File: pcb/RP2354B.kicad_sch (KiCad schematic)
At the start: 29 parts, among them J1 Conn_01x03_MountingPin, SW1 SW_Push, SW2 SW_Push, U2 RP2354B, Y1 ABM8-272-T3

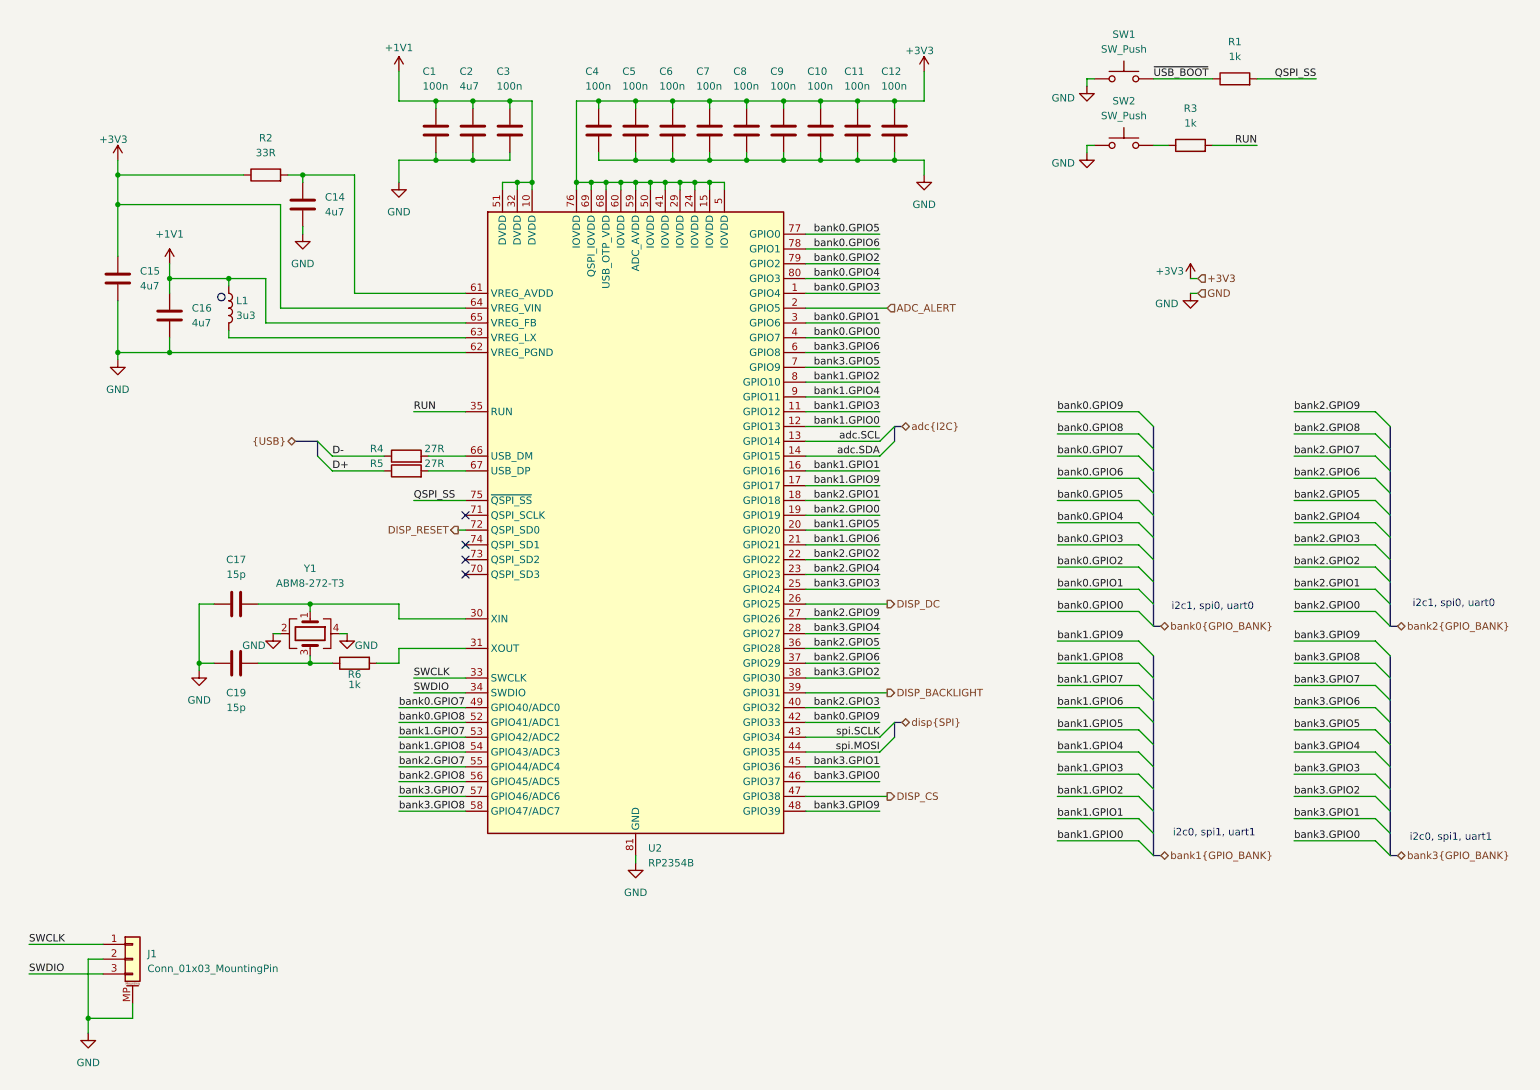
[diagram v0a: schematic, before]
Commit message: finished rough schematic
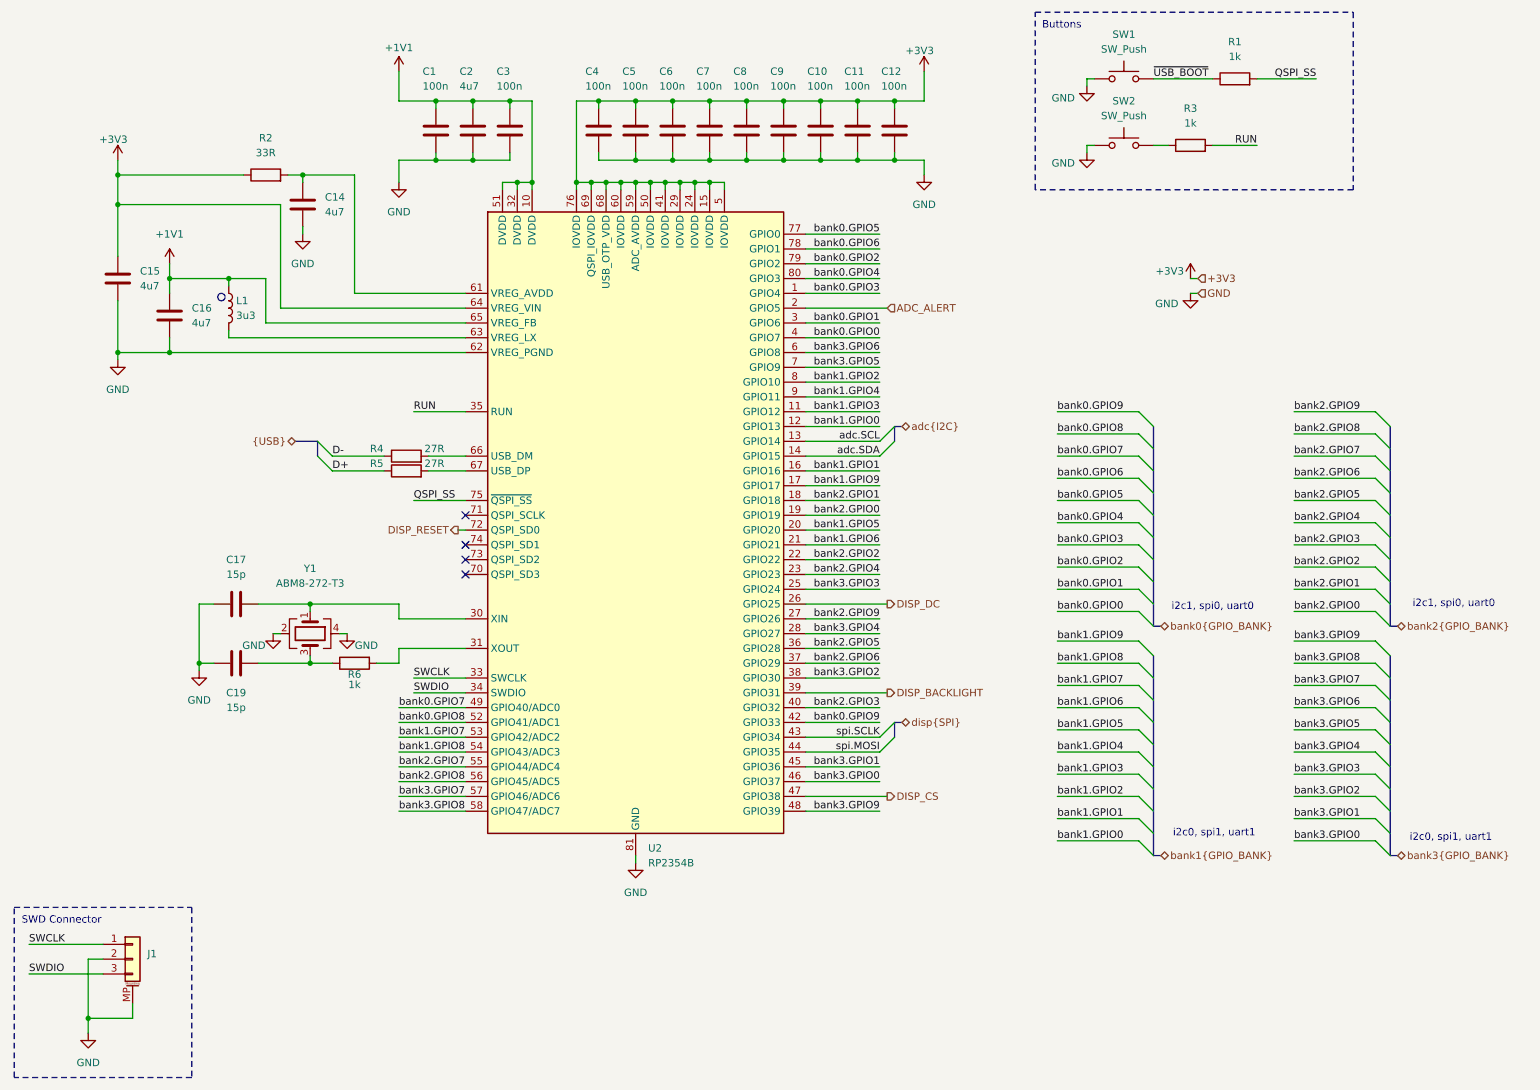
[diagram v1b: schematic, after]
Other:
- note added: "Buttons"
- note added: "SWD Connector"
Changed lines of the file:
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@@
 	(generator_version "10.0")
 	(paper "A4")
+	(rectangle
+		(start 189.23 13.97)
+		(end 243.84 44.45)
+		(stroke
+			(width 0.2032)
+			(type dash)
+		)
+		(fill
+			(type none)
+		)
+	)
+	(rectangle
+		(start 13.97 167.64)
+		(end 44.45 196.85)
+		(stroke
+			(width 0.2032)
+			(type dash)
+		)
+		(fill
+			(type none)
+		)
+	)
 	(circle
 		(center 49.53 62.865)
@@
 		)
 	)
+	(text "Buttons"
+		(exclude_from_sim no)
+		(at 193.802 16.256 0)
+		(effects
+			(font
+				(size 1.27 1.27)
+			)
+		)
+	)
 	(text "i2c1, spi0, uart0"
 		(exclude_from_sim no)
@@
 		)
 	)
+	(text "SWD Connector"
+		(exclude_from_sim no)
+		(at 22.098 169.926 0)
+		(effects
+			(font
+				(size 1.27 1.27)
+			)
+		)
+	)
 	(junction
 		(at 99.06 29.21)
@@
 		(property "Value" "Conn_01x03_MountingPin"
 			(at 36.83 178.1555 0)
+			(hide yes)
 			(show_name no)
 			(do_not_autoplace no)

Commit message: did more layout, added 3d models
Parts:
- R1, R3: footprint Resistor_SMD:R_0603_1608Metric -> Resistor_SMD:R_0402_1005Metric
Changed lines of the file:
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@@
 			)
 		)
-		(property "Footprint" "Resistor_SMD:R_0603_1608Metric"
+		(property "Footprint" "Resistor_SMD:R_0402_1005Metric"
 			(at 223.52 27.178 90)
 			(hide yes)
@@
 			)
 		)
-		(property "Footprint" "Resistor_SMD:R_0603_1608Metric"
+		(property "Footprint" "Resistor_SMD:R_0402_1005Metric"
 			(at 215.9 38.608 90)
 			(hide yes)

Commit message: changed out footprints
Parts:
- C15, C16: footprint Capacitor_SMD:C_0402_1005Metric -> RP2354B_MINIMAL:C_0402_1005Metric_small_pads
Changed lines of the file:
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@@
 			)
 		)
-		(property "Footprint" "Capacitor_SMD:C_0402_1005Metric"
+		(property "Footprint" "RP2354B_MINIMAL:C_0402_1005Metric_small_pads"
 			(at 32.7152 63.5 0)
 			(hide yes)
@@
 			)
 		)
-		(property "Footprint" "Capacitor_SMD:C_0402_1005Metric"
+		(property "Footprint" "RP2354B_MINIMAL:C_0402_1005Metric_small_pads"
 			(at 41.6052 69.85 0)
 			(hide yes)

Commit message: worked on the pcb
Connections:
- net spi.MOSI renamed disp.MOSI
- net spi.SCLK renamed disp.SCLK
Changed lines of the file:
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@@
 		)
 	)
-	(label "spi.SCLK"
+	(label "disp.SCLK"
 		(at 162.56 138.43 180)
 		(effects
@@
 		)
 	)
-	(label "spi.MOSI"
+	(label "disp.MOSI"
 		(at 162.56 140.97 180)
 		(effects

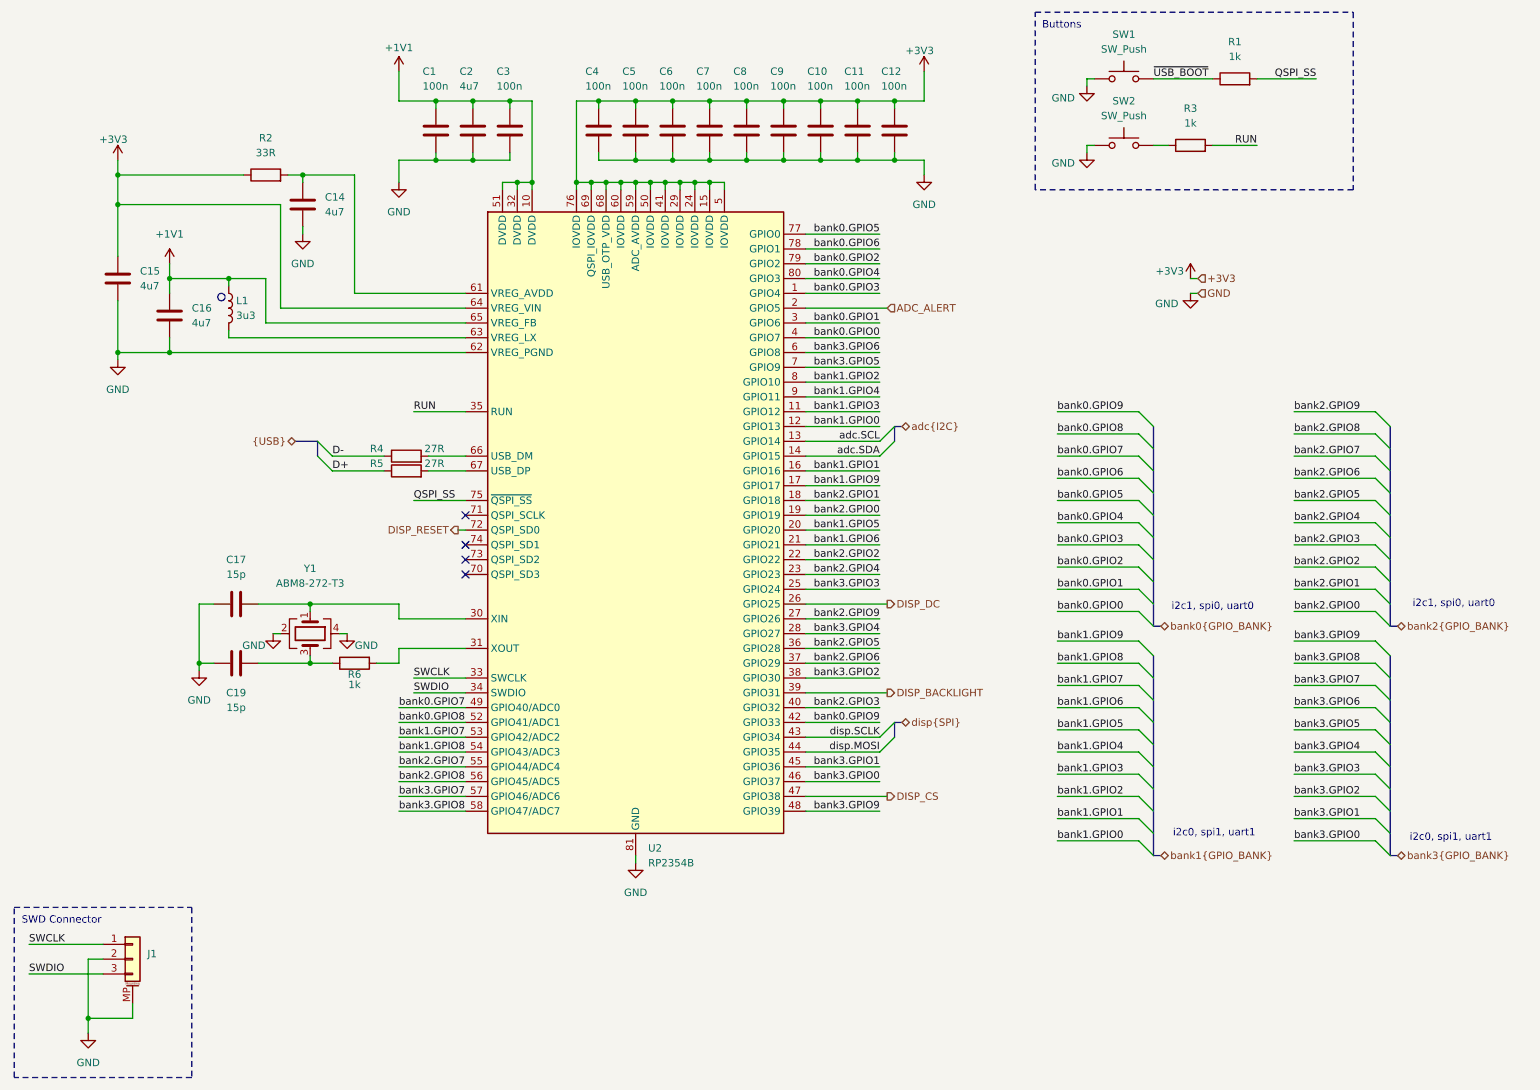
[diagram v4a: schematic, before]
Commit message: swapped the module pins around
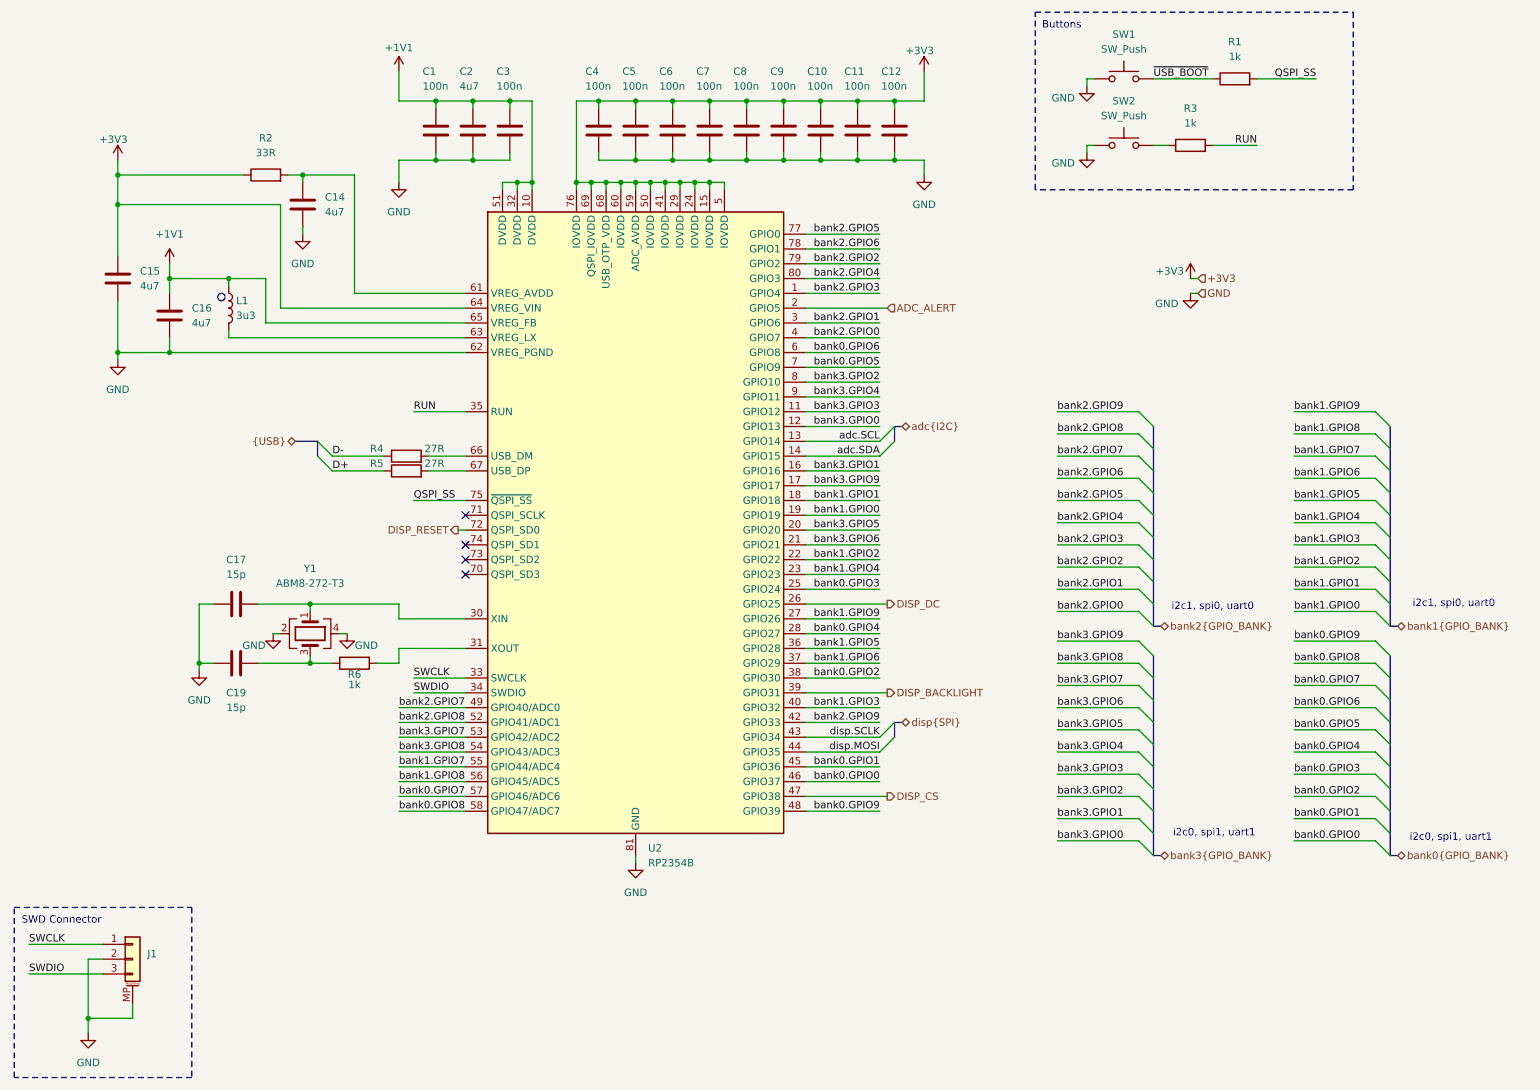
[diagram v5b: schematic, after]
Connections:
- net bank0.GPIO0: now also U2.46 (GPIO37); no longer U2.4 (GPIO7)
- net bank0.GPIO1: now also U2.45 (GPIO36); no longer U2.3 (GPIO6)
- net bank0.GPIO2: now also U2.38 (GPIO30); no longer U2.79 (GPIO2)
- net bank0.GPIO3: now also U2.25 (GPIO24); no longer U2.1 (GPIO4)
- net bank0.GPIO4: now also U2.28 (GPIO27); no longer U2.80 (GPIO3)
- net bank0.GPIO5: now also U2.7 (GPIO9); no longer U2.77 (GPIO0)
- net bank0.GPIO6: now also U2.6 (GPIO8); no longer U2.78 (GPIO1)
- net bank0.GPIO7: now also U2.57 (GPIO46/ADC6); no longer U2.49 (GPIO40/ADC0)
- net bank0.GPIO8: now also U2.58 (GPIO47/ADC7); no longer U2.52 (GPIO41/ADC1)
- net bank0.GPIO9: now also U2.48 (GPIO39); no longer U2.42 (GPIO33)
- net bank1.GPIO0: now also U2.19 (GPIO19); no longer U2.12 (GPIO13)
- net bank1.GPIO1: now also U2.18 (GPIO18); no longer U2.16 (GPIO16)
- net bank1.GPIO2: now also U2.22 (GPIO22); no longer U2.8 (GPIO10)
- net bank1.GPIO3: now also U2.40 (GPIO32); no longer U2.11 (GPIO12)
- net bank1.GPIO4: now also U2.23 (GPIO23); no longer U2.9 (GPIO11)
- net bank1.GPIO5: now also U2.36 (GPIO28); no longer U2.20 (GPIO20)
- net bank1.GPIO6: now also U2.37 (GPIO29); no longer U2.21 (GPIO21)
- net bank1.GPIO7: now also U2.55 (GPIO44/ADC4); no longer U2.53 (GPIO42/ADC2)
- net bank1.GPIO8: now also U2.56 (GPIO45/ADC5); no longer U2.54 (GPIO43/ADC3)
- net bank1.GPIO9: now also U2.27 (GPIO26); no longer U2.17 (GPIO17)
- net bank2.GPIO0: now also U2.4 (GPIO7); no longer U2.19 (GPIO19)
- net bank2.GPIO1: now also U2.3 (GPIO6); no longer U2.18 (GPIO18)
- net bank2.GPIO2: now also U2.79 (GPIO2); no longer U2.22 (GPIO22)
- net bank2.GPIO3: now also U2.1 (GPIO4); no longer U2.40 (GPIO32)
- net bank2.GPIO4: now also U2.80 (GPIO3); no longer U2.23 (GPIO23)
- net bank2.GPIO5: now also U2.77 (GPIO0); no longer U2.36 (GPIO28)
- net bank2.GPIO6: now also U2.78 (GPIO1); no longer U2.37 (GPIO29)
- net bank2.GPIO7: now also U2.49 (GPIO40/ADC0); no longer U2.55 (GPIO44/ADC4)
- net bank2.GPIO8: now also U2.52 (GPIO41/ADC1); no longer U2.56 (GPIO45/ADC5)
- net bank2.GPIO9: now also U2.42 (GPIO33); no longer U2.27 (GPIO26)
- net bank3.GPIO0: now also U2.12 (GPIO13); no longer U2.46 (GPIO37)
- net bank3.GPIO1: now also U2.16 (GPIO16); no longer U2.45 (GPIO36)
- net bank3.GPIO2: now also U2.8 (GPIO10); no longer U2.38 (GPIO30)
- net bank3.GPIO3: now also U2.11 (GPIO12); no longer U2.25 (GPIO24)
- net bank3.GPIO4: now also U2.9 (GPIO11); no longer U2.28 (GPIO27)
- net bank3.GPIO5: now also U2.20 (GPIO20); no longer U2.7 (GPIO9)
- net bank3.GPIO6: now also U2.21 (GPIO21); no longer U2.6 (GPIO8)
- net bank3.GPIO7: now also U2.53 (GPIO42/ADC2); no longer U2.57 (GPIO46/ADC6)
- net bank3.GPIO8: now also U2.54 (GPIO43/ADC3); no longer U2.58 (GPIO47/ADC7)
- net bank3.GPIO9: now also U2.17 (GPIO17); no longer U2.48 (GPIO39)

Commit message: added test points
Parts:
- added TP11, TP12, TP13, TP14: TestPoint, TestPoint:TestPoint_Pad_D1.0mm, symbol Connector:TestPoint
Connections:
- net at U2.70 (QSPI_SD3): now also TP14.1
- net at U2.71 (QSPI_SCLK): now also TP11.1
- net at U2.73 (QSPI_SD2): now also TP13.1
- net at U2.74 (QSPI_SD1): now also TP12.1
- no-connect marks 4 -> 0
